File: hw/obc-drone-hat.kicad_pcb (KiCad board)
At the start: 4 copper layers, 65 x 56.5 mm, 69 parts, among them SW1 SW_DIP_x04

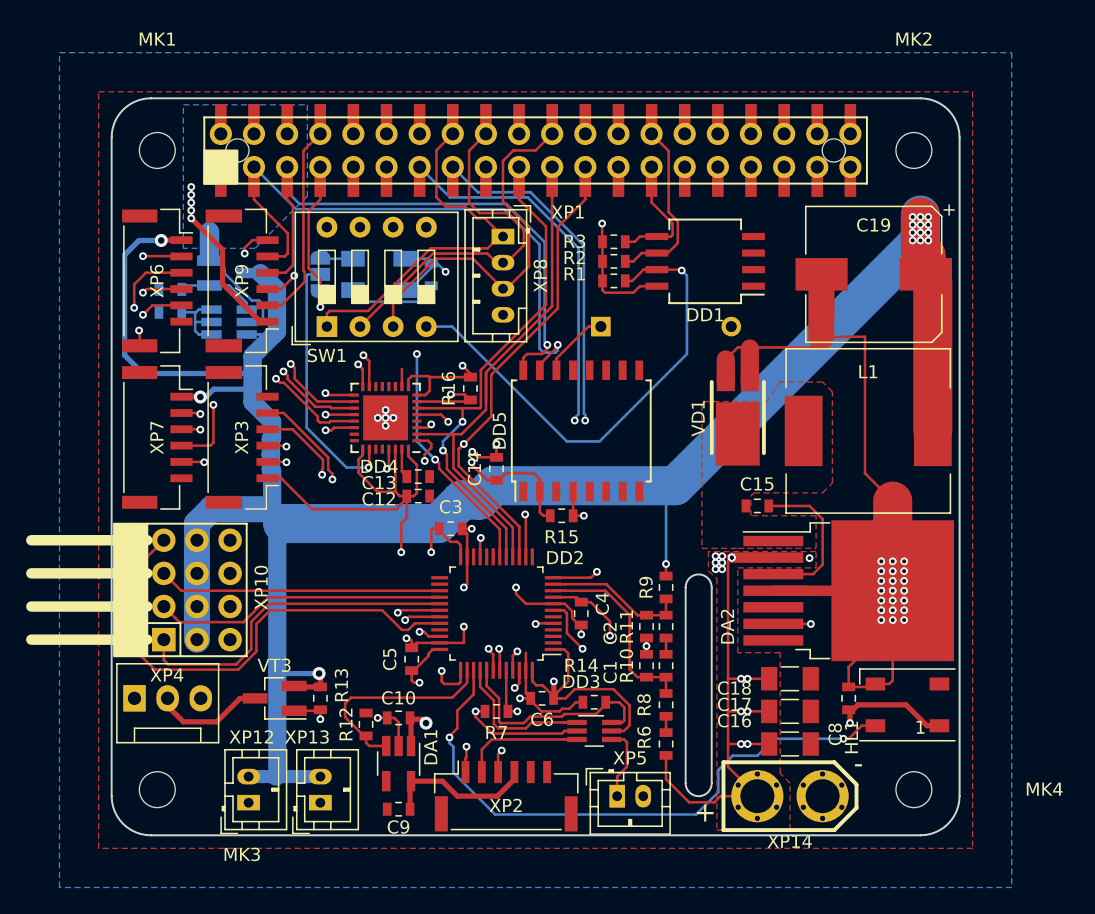
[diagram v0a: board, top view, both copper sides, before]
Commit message: rebuild as serio/pario hat
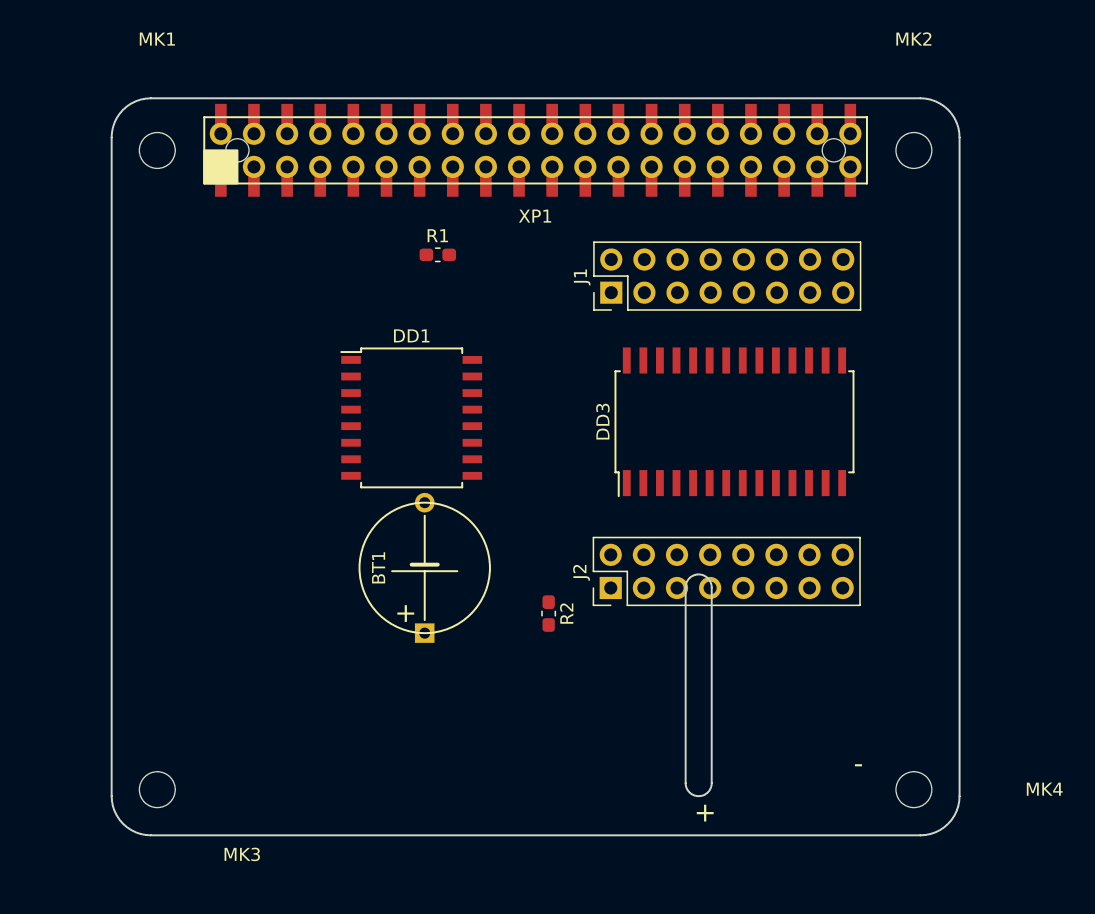
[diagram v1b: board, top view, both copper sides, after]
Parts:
- removed C1, C10, C11, C12, C13, C14, C2, C3, C4, C5, C6, C8, C9: 0.1, Capacitor_SMD:C_0603_1608Metric
- removed C15: 0.01, Capacitor_SMD:C_0603_1608Metric
- removed C16, C17: 10.0 50V, Capacitor_SMD:C_1206_3216Metric_Pad1.24x1.80mm_HandSolder
- removed C18: 0.47, Capacitor_SMD:C_1206_3216Metric_Pad1.24x1.80mm_HandSolder
- removed C19: 1000.0 uF 10 V, Capacitor_SMD:CP_Elec_10x10.5
- removed DA1: NCP361SN, Package_TO_SOT_SMD:SOT-23-5_HandSoldering
- removed DA2: LM2678SX-5.0/NOPB, Package_TO_SOT_SMD:TO-263-7_TabPin4
- removed DD2: STM32F030CCTx, Package_QFP:LQFP-48_7x7mm_P0.5mm
- removed DD4: MAX3109, Package_DFN_QFN:QFN-32-1EP_5x5mm_P0.5mm_EP3.45x3.45mm
- removed DD5: DS3231, Package_SO:SOIC-16W_7.5x10.3mm_P1.27mm
- removed HL1: WS2812B, LED_SMD:LED_WS2812B_PLCC4_5.0x5.0mm_P3.2mm
- removed JP1: Jumper_3_Open, Jumper:SolderJumper-3_P1.3mm_Open_RoundedPad1.0x1.5mm
- removed L1: 12 uH SRR1208-120ML, Inductor_SMD:L_12x12mm_H8mm
- removed R10, R11, R12, R14, R16, R4, R7, R9: 10k, Resistor_SMD:R_0603_1608Metric
- removed R13: 4.7k, Resistor_SMD:R_0603_1608Metric
- removed R15: nc, Resistor_SMD:R_0603_1608Metric
- removed R3: 3.9k, Resistor_SMD:R_0603_1608Metric
- removed R5, R6, R8: 47k, Resistor_SMD:R_0603_1608Metric
- removed REF**: OSHW-Logo2_14.6x12mm_SilkScreen, Symbol:OSHW-Logo2_14.6x12mm_SilkScreen
- removed SW1: SW_DIP_x04, Button_Switch_THT:SW_DIP_SPSTx04_Slide_9.78x12.34mm_W7.62mm_P2.54mm
- removed VD1: PDS760-13, hat:D-PowerDI-5
- removed VT1, VT3: DMG2305UX, Package_TO_SOT_SMD:SOT-23_Handsoldering
- removed VT2: DMMT5401, Package_TO_SOT_SMD:SOT-23-6_Handsoldering
- removed XP10: SERVO, hat:SERVO4
- removed XP12, XP13: PWR-5V, Connector_JST:JST_PH_B2B-PH-K_1x02_P2.00mm_Vertical
- removed XP14: BATT, hat:XT30
- removed XP2: FrSky-XSR, Connector_JST:JST_GH_SM06B-GHS-TB_1x06-1MP_P1.25mm_Horizontal
- removed XP3: DC-Debug, Connector_JST:JST_GH_BM06B-GHS-TBT_1x06-1MP_P1.25mm_Vertical
- removed XP4: FAN, Connector:FanPinHeader_1x03_P2.54mm_Vertical
- removed XP5: CPPM OUT, Connector_JST:JST_PH_B2B-PH-K_1x02_P2.00mm_Vertical
- removed XP6: TELEM1, Connector_JST:JST_GH_SM06B-GHS-TB_1x06-1MP_P1.25mm_Horizontal
- removed XP7: TELEM2, Connector_JST:JST_GH_SM06B-GHS-TB_1x06-1MP_P1.25mm_Horizontal
- removed XP8: CFG ID, Connector_JST:JST_PH_B4B-PH-K_1x04_P2.00mm_Vertical
- removed XP9: RPI-CON, Connector_JST:JST_GH_BM06B-GHS-TBT_1x06-1MP_P1.25mm_Vertical
- removed ZQ1: ASFL1-24.000MHZ-EC-T, Crystal:Crystal_SMD_Abracon_ABM3B-4Pin_5.0x3.2mm
- added J1: Conn_02x08_Top_Bottom, Connector_PinHeader_2.54mm:PinHeader_2x08_P2.54mm_Vertical, F.Cu at (168.3, 98.4)
- added J2: Conn_02x08_Top_Bottom, Connector_PinHeader_2.54mm:PinHeader_2x08_P2.54mm_Vertical, F.Cu at (168.3, 121.0)
- BT1: moved to F.Cu
- DD1: value CAT24C256WI-GT3 -> DS3231; footprint Package_SO:SO-8_5.3x6.2mm_P1.27mm -> Package_SO:SOIC-16W_7.5x10.3mm_P1.27mm
- DD3: value NC7SZ157P6X -> MCP23S17; footprint Package_TO_SOT_SMD:SOT-363_SC-70-6_Handsoldering -> Package_SO:SOIC-28W_7.5x17.9mm_P1.27mm
- R1: value 1k -> 10k; footprint Resistor_SMD:R_0603_1608Metric -> Resistor_SMD:R_0603_1608Metric_Pad1.05x0.95mm_HandSolder
- R2: value 3.9k -> nc; footprint Resistor_SMD:R_0603_1608Metric -> Resistor_SMD:R_0603_1608Metric_Pad1.05x0.95mm_HandSolder
- moved R2 27.5 mm to (163.5, 123.0), turned to 270 degrees
- moved BT1 26.2 mm to (154.0, 119.5), turned to 90 degrees
- moved DD3 26.0 mm to (177.7, 108.3), turned to 90 degrees
- moved DD1 25.5 mm to (153.0, 108.0), turned to 0 degrees
- moved R1 13.6 mm to (155.0, 95.5)
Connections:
- net +5VP renamed +5V
- BT1 pad 1: /RTC/+3Vbat -> /+3Vbat
- BT1 pad 2: GND -> Net-(BT1-Pad2)
- DD1 pad 1: GND -> Net-(DD1-Pad1)
- DD1 pad 2: GND -> +3V3
- DD1 pad 3: GND -> Net-(DD1-Pad3)
- DD1 pad 4: GND -> ~HAT_RST
- DD1 pad 5: /RPi/ID_SDA -> Net-(DD1-Pad5)
- DD1 pad 6: /RPi/ID_SCL -> Net-(DD1-Pad6)
- DD1 pad 7: ~HAT_ID_WE -> Net-(DD1-Pad7)
- DD1 pad 8: +3.3VP -> Net-(DD1-Pad8)
- DD3 pad 1: /RC IO MCU/STM_CPPM -> Net-(DD3-Pad1)
- DD3 pad 2: GND -> Net-(DD3-Pad2)
- DD3 pad 3: /RC IO MCU/Rx_CPPM -> Net-(DD3-Pad3)
- DD3 pad 4: /RC IO MCU/CPPM_OUT -> Net-(DD3-Pad4)
- DD3 pad 5: +3.3VP -> Net-(DD3-Pad5)
- DD3 pad 6: /RC IO MCU/CPPM_SEL -> Net-(DD3-Pad6)
- R1 pad 1: +3.3VP -> ~SER_IRQ_A
- R1 pad 2: ~HAT_ID_WE -> +3V3
- R2 pad 1: +3.3VP -> ~HAT_RST
- R2 pad 2: /RPi/ID_SCL -> +3V3
- XP1 pad 1: +3.3VP -> +3V3
- XP1 pad 10: RPI_RX -> Net-(XP1-Pad10)
- XP1 pad 11: ~SER_IRQ -> ~SER_IRQ_A
- XP1 pad 12: ~STM_INT -> Net-(XP1-Pad12)
- XP1 pad 13: ~STM_RESET -> Net-(XP1-Pad13)
- XP1 pad 15: STM_BOOT0 -> Net-(XP1-Pad15)
- XP1 pad 16: CFG_ID0 -> Net-(XP1-Pad16)
- XP1 pad 17: +3.3VP -> +3V3
- XP1 pad 18: CFG_ID1 -> Net-(XP1-Pad18)
- XP1 pad 22: CFG_ID2 -> Net-(XP1-Pad22)
- XP1 pad 24: ~RPI_SPI0_CE0 -> /CE0
- XP1 pad 26: ~RPI_SPI0_CE1 -> /CE1
- XP1 pad 27: /RPi/ID_SDA -> Net-(XP1-Pad27)
- XP1 pad 28: /RPi/ID_SCL -> Net-(XP1-Pad28)
- XP1 pad 8: RPI_TX -> Net-(XP1-Pad8)
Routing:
- net +5Vhat: track 296.6 -> 0.00 mm, vias 18 -> 0
- net +3.3VP: track 210.8 -> 0.00 mm, vias 9 -> 0
- net GND: track 167.9 -> 7.25 mm, vias 41 -> 0
- net +5V: track 77.5 -> 2.90 mm, vias 6 -> 0
- net RPI_SDA: track 73.1 -> 0.00 mm, vias 2 -> 0
- net RPI_SCL: track 71.5 -> 0.00 mm, vias 2 -> 0
- net STM_BOOT0: track 61.5 -> 0.00 mm, vias 2 -> 0
- net ~STM_RESET: track 54.3 -> 0.00 mm, vias 2 -> 0
- net /RC IO MCU/WS_DOUT: track 46.2 -> 0.00 mm, vias 2 -> 0
- net Vbat: track 45.0 -> 0.00 mm, vias 15 -> 0
- net HAT_CLK: track 39.3 -> 0.00 mm, vias 2 -> 0
- net RPI_SPI0_SCLK: track 40.7 -> 1.45 mm, vias 2 -> 0
- net RPI_SPI0_MISO: track 40.4 -> 1.45 mm
- net RPI_SPI0_MOSI: track 40.3 -> 1.45 mm, vias 2 -> 0
- net ~HAT_ID_WE: track 37.7 -> 0.00 mm, vias 1 -> 0
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- removed copper zone on B.Cu, net +5V
- removed copper zone on In1.Cu, net +5V
- removed copper zone on F.Cu, net /DC-DC/VSW
- removed copper zone on B.Cu, net GND
- removed copper zone on F.Cu, net GND
- removed copper zone on In1.Cu, net GND
- removed copper zone on In2.Cu, net GND
- removed copper zone on F.Cu, net Vbat
- removed copper zone on In1.Cu, net Vbat
